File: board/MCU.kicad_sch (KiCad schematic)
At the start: 3 parts, among them J1 RJ45_LED_Shielded, U1 Teensy4.1_DEV-16771

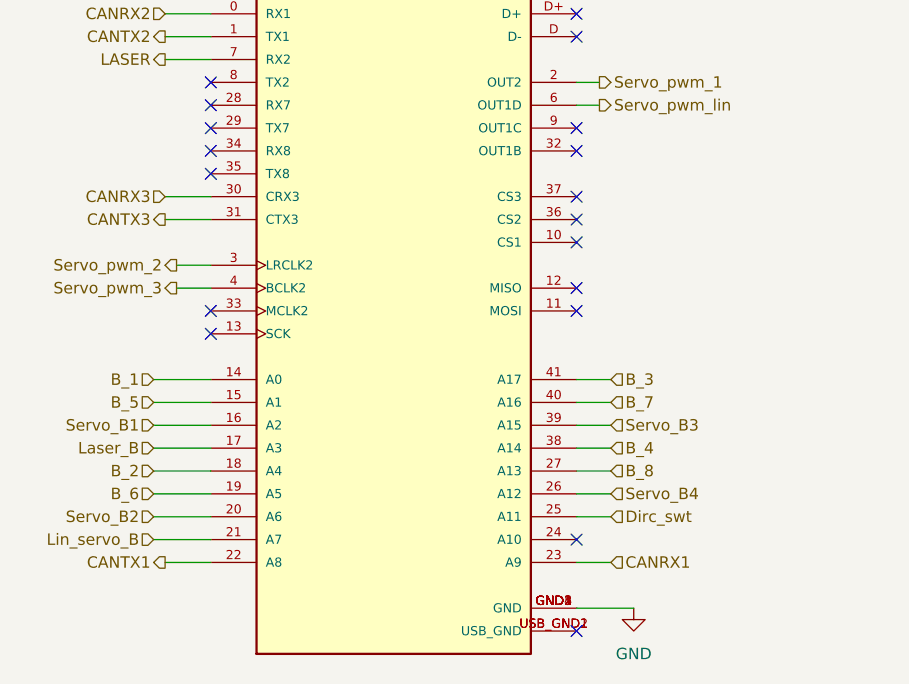
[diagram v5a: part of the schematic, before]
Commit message: Began Traces and shrunk board complete redesign
Complete3ly redid the board to be smaller and make traces
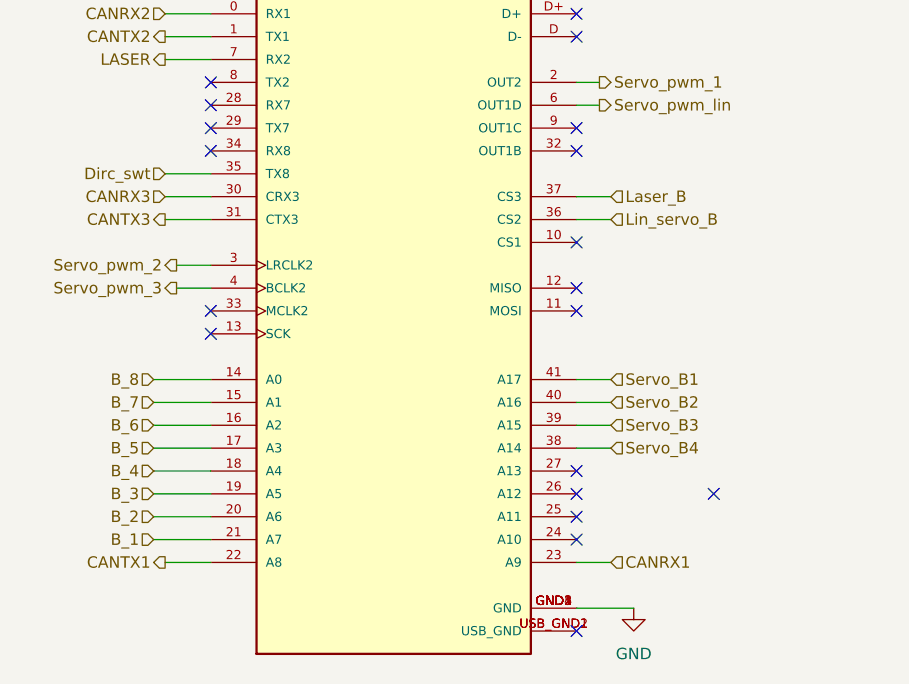
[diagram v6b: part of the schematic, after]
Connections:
- net B_1: now also U1.21 (A7); no longer U1.14 (A0)
- net B_2: now also U1.20 (A6); no longer U1.18 (A4)
- net B_3: now also U1.19 (A5); no longer U1.41 (A17)
- net B_4: now also U1.18 (A4); no longer U1.38 (A14)
- net B_5: now also U1.17 (A3); no longer U1.15 (A1)
- net B_6: now also U1.16 (A2); no longer U1.19 (A5)
- net B_7: now also U1.15 (A1); no longer U1.40 (A16)
- net B_8: now also U1.14 (A0); no longer U1.27 (A13)
- net Dirc_swt: now also U1.35 (TX8); no longer U1.25 (A11)
- net Laser_B: now also U1.37 (CS3); no longer U1.17 (A3)
- net Lin_servo_B: now also U1.36 (CS2); no longer U1.21 (A7)
- net Servo_B1: now also U1.41 (A17); no longer U1.16 (A2)
- net Servo_B2: now also U1.40 (A16); no longer U1.20 (A6)
- net Servo_B4: now also U1.38 (A14); no longer U1.26 (A12)
- no-connect marks 27 -> 28

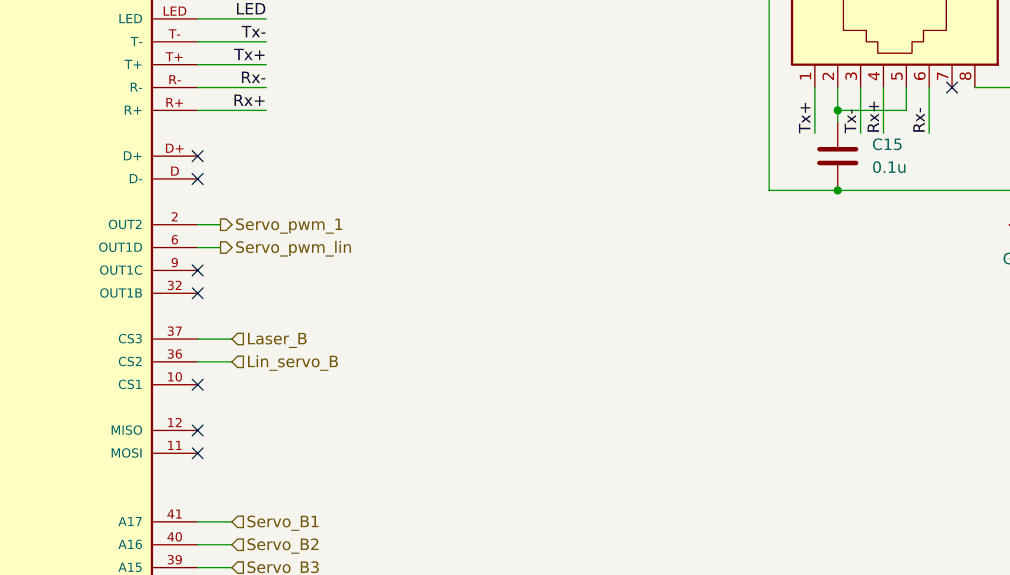
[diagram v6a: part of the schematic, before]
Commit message: Fix reverse voltage protection circuit
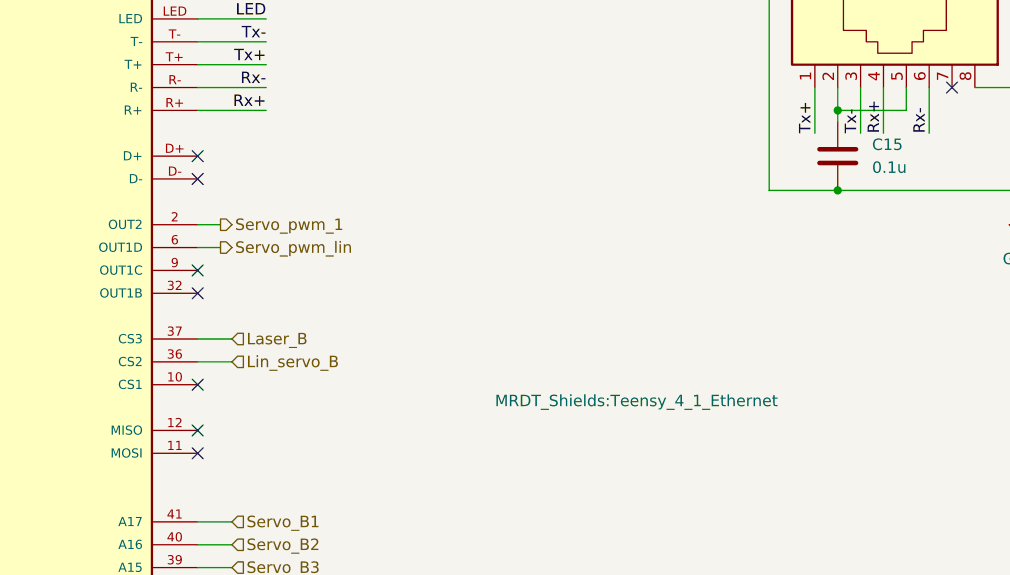
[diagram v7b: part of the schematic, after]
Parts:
- U1: footprint MRDT_Shields:Teensy_4_1 -> MRDT_Shields:Teensy_4_1_Ethernet
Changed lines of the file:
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@@
 			)
 		)
-		(property "Footprint" "MRDT_Shields:Teensy_4_1"
+		(property "Footprint" "MRDT_Shields:Teensy_4_1_Ethernet"
 			(at 139.7 101.6 0)
 			(effects
@@
 				)
 				(justify left bottom)
-				(hide yes)
 			)
 		)
@@
 		(pin "T-"
 		)
-		(pin "D"
+		(pin "D-"
 		)
 		(pin "T+"
